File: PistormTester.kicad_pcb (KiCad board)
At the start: 2 copper layers, 100.1 x 99.8 mm, 88 parts, among them J1 USB_B_Micro, J2 Conn_02x12_Odd_Even, J3 Conn_01x06_Female, J4 Conn_01x16_Female, J5 Conn_01x16_Female, J6 Conn_01x16_Female, J7 Conn_02x13_Odd_Even, J8 Conn_01x13, J9 Conn_01x02, U2 68000D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

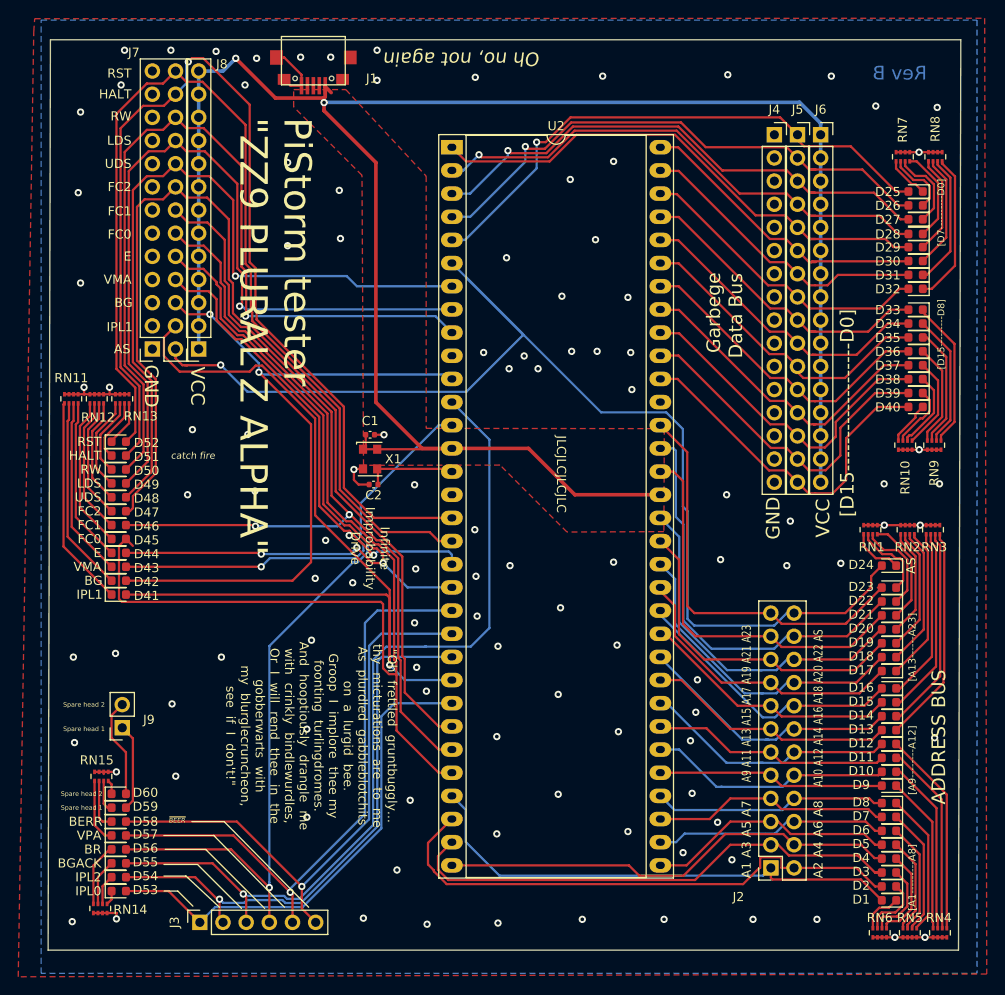
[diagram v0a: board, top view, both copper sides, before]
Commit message: fixed PCB outline wonk. updated to Rev C
Rev B has been sent to production to further changes are now Rev C
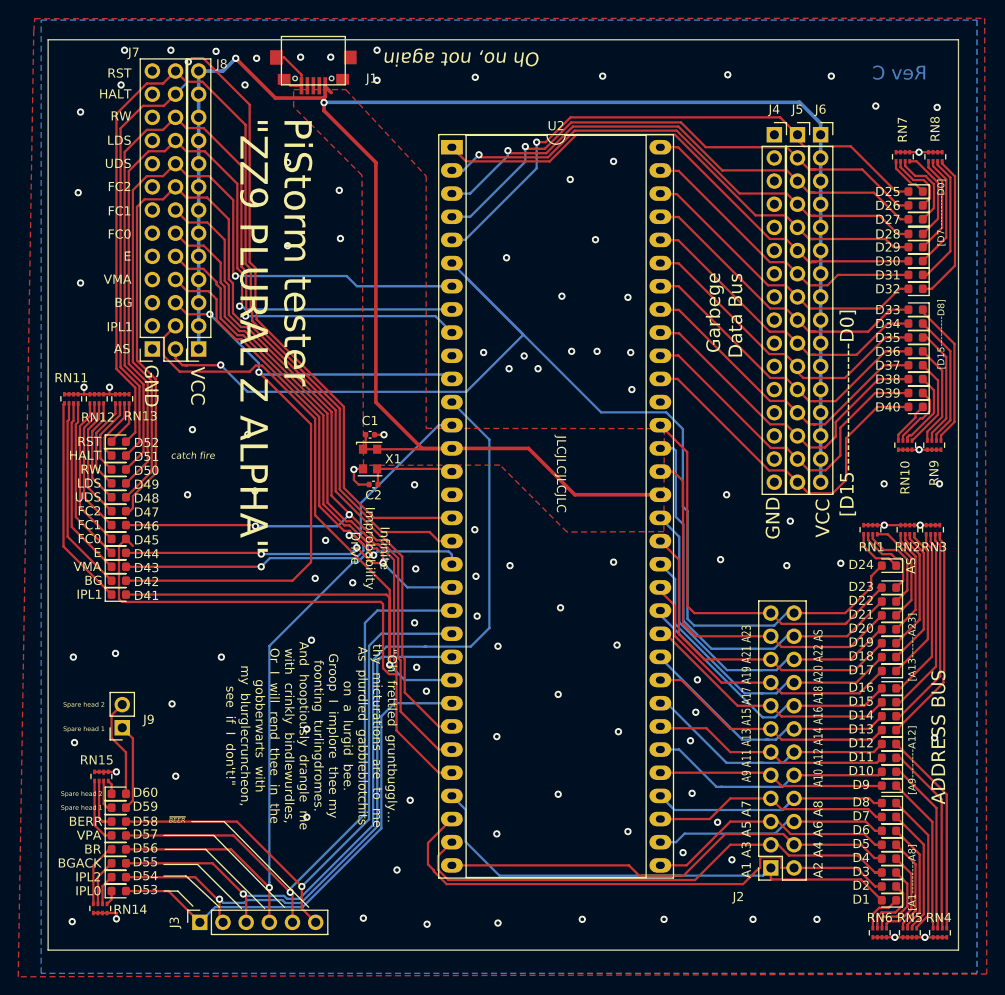
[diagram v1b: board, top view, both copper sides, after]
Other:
- board size 100.1 x 99.8 mm -> 99.8 x 99.8 mm
- board text added: "Rev C"
- board text removed: "Rev B"

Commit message: REV C - Fixed ZIF holes
Made the holes for the 68K socket significantly bigger (and moved slightly inboard) to better accommodate ZIF sockets with silly big pins.
minor re-routing of a few signals too.
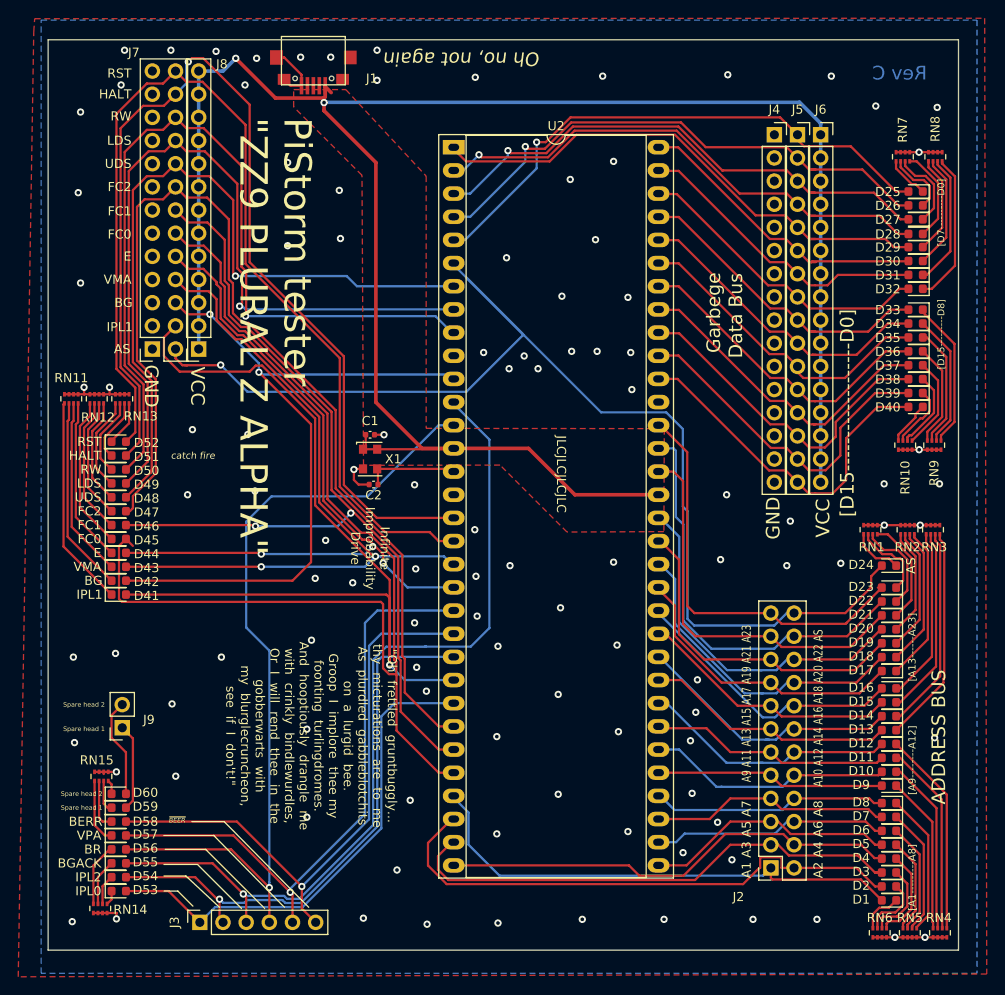
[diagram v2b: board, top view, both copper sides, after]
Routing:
- net /BR: track 82.0 -> 89.4 mm
- net /VMA: track 81.6 -> 78.3 mm, vias 3 -> 2
- net /E: track 82.9 -> 81.3 mm

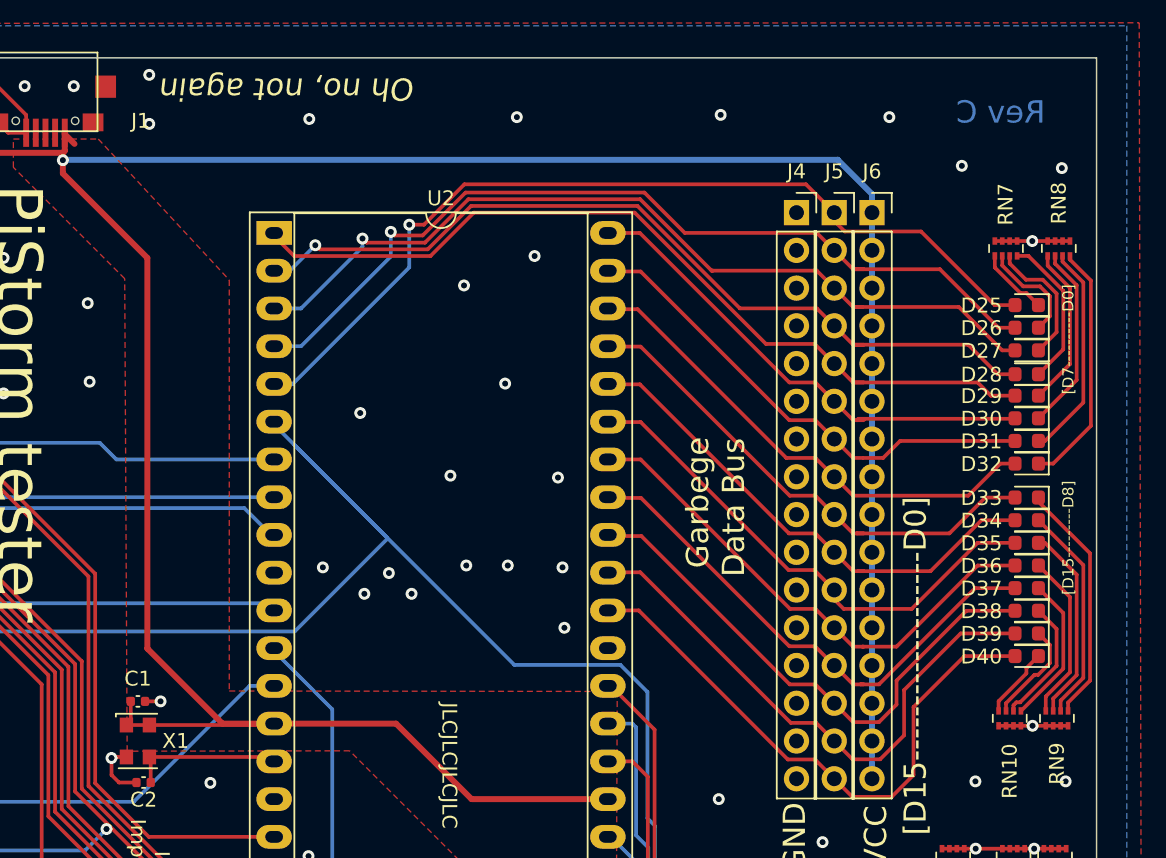
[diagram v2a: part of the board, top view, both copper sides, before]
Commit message: Change to a 3.3v oscillator RevC.1
switched to a 3.3v Oscillator and an associated 3.3v regulator
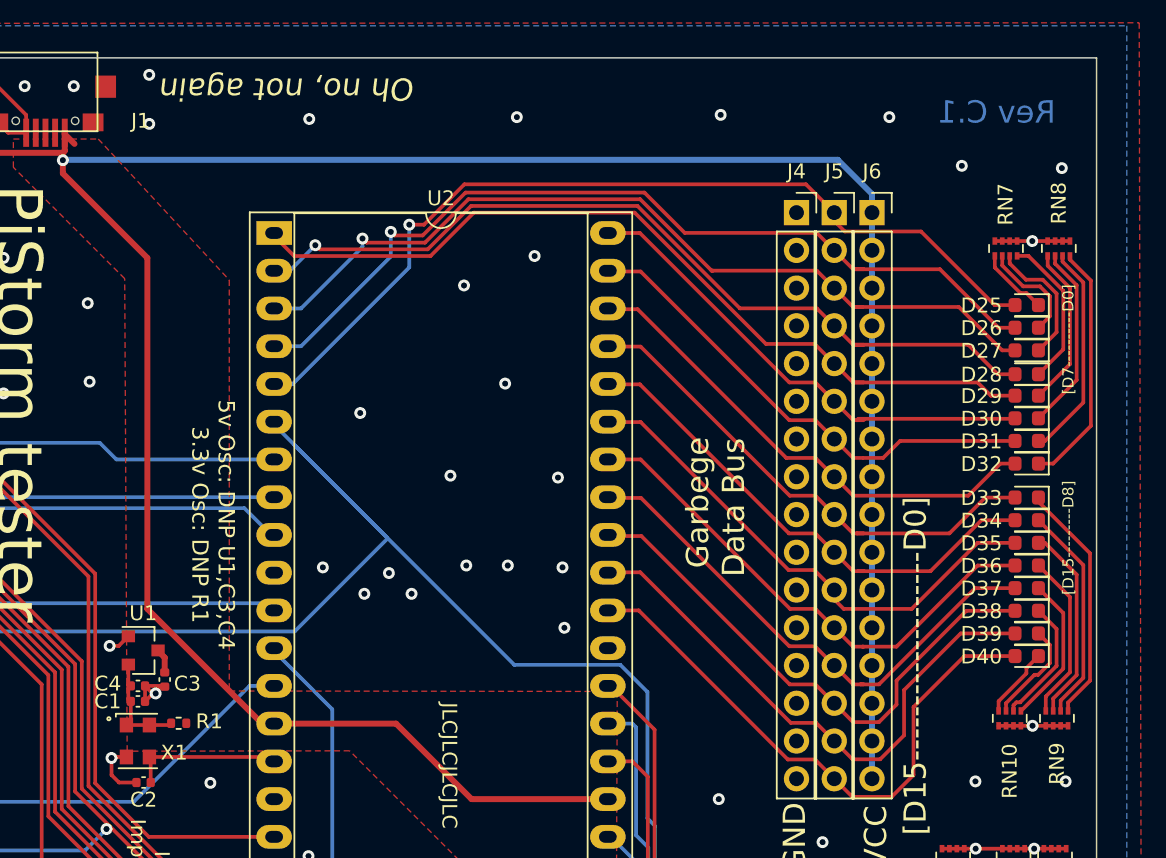
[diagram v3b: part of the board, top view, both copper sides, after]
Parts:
- added C3: 1uF, Capacitor_SMD:C_0402_1005Metric, F.Cu at (121.7, 98.4)
- added C4: 1uF, Capacitor_SMD:C_0402_1005Metric, F.Cu at (119.9, 98.8)
- added R1: 0 R, Resistor_SMD:R_0402_1005Metric, F.Cu at (122.6, 101.3)
- added U1: AP2127N-1.0, Package_TO_SOT_SMD:SOT-23, F.Cu at (120.2, 96.4)
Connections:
- C1 pad 1: +5V -> VCC
- X1 pad 1: +5V -> VCC
- X1 pad 4: +5V -> VCC
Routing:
- net +5V: track 227.5 -> 215.1 mm
- net VCC: track 0.00 -> 7.61 mm
- net GND: track 52.4 -> 58.5 mm, vias 109 -> 110
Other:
- board text added: "5v Osc: DNP U1,C3,C4 3.3v Osc: DNP R1"
- board text added: "Rev C.1"
- board text removed: "Rev C"
